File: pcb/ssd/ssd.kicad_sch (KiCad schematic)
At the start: 0 parts

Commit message: 将USB电源升级为5-12V双路DCDC
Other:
- note added: "USB-C 接口与电源 5～12V 输入、5V / 3.3V DCDC"
- note added: "主控：STM32C562CET6，LQFP48，512KB 闪存 / 128KB 运行内存。 VBUS 按外部 5～12V 输入设计；标准 5V USB 连接可用于 ROM DFU。"
- note removed: "USB-C 接口与电源 5V 输入、3.3V 稳压"
- note removed: "主控：STM32C562CET6，LQFP48，512KB 闪存 / 128KB 运行内存。 USB-C 同时用于 5V 供电和出厂引导程序 USB DFU 烧录。"
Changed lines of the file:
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@@
 	(title_block
 		(title "STM32C562 温度与流量显示系统")
-		(date "2026-09-16")
-		(rev "A2")
+		(date "2026-09-18")
+		(rev "A3")
 		(company "温度与流量显示项目")
-		(comment 1 "STM32C562 最小系统与外围电路；全部电阻、电容采用 0603")
+		(comment 1 "常规阻容采用 0603；DCDC 储能电容采用 1206")
 	)
 	(polyline
@@
 		)
 	)
-	(text "主控：STM32C562CET6，LQFP48，512KB 闪存 / 128KB 运行内存。\nUSB-C 同时用于 5V 供电和出厂引导程序 USB DFU 烧录。"
+	(text "主控：STM32C562CET6，LQFP48，512KB 闪存 / 128KB 运行内存。\nVBUS 按外部 5～12V 输入设计；标准 5V USB 连接可用于 ROM DFU。"
 		(exclude_from_sim no)
 		(at 20 33 0)
@@
 		)
 	)
-	(text "USB-C 接口与电源\n5V 输入、3.3V 稳压"
+	(text "USB-C 接口与电源\n5～12V 输入、5V / 3.3V DCDC"
 		(exclude_from_sim no)
 		(at 31.75 78.74 0)

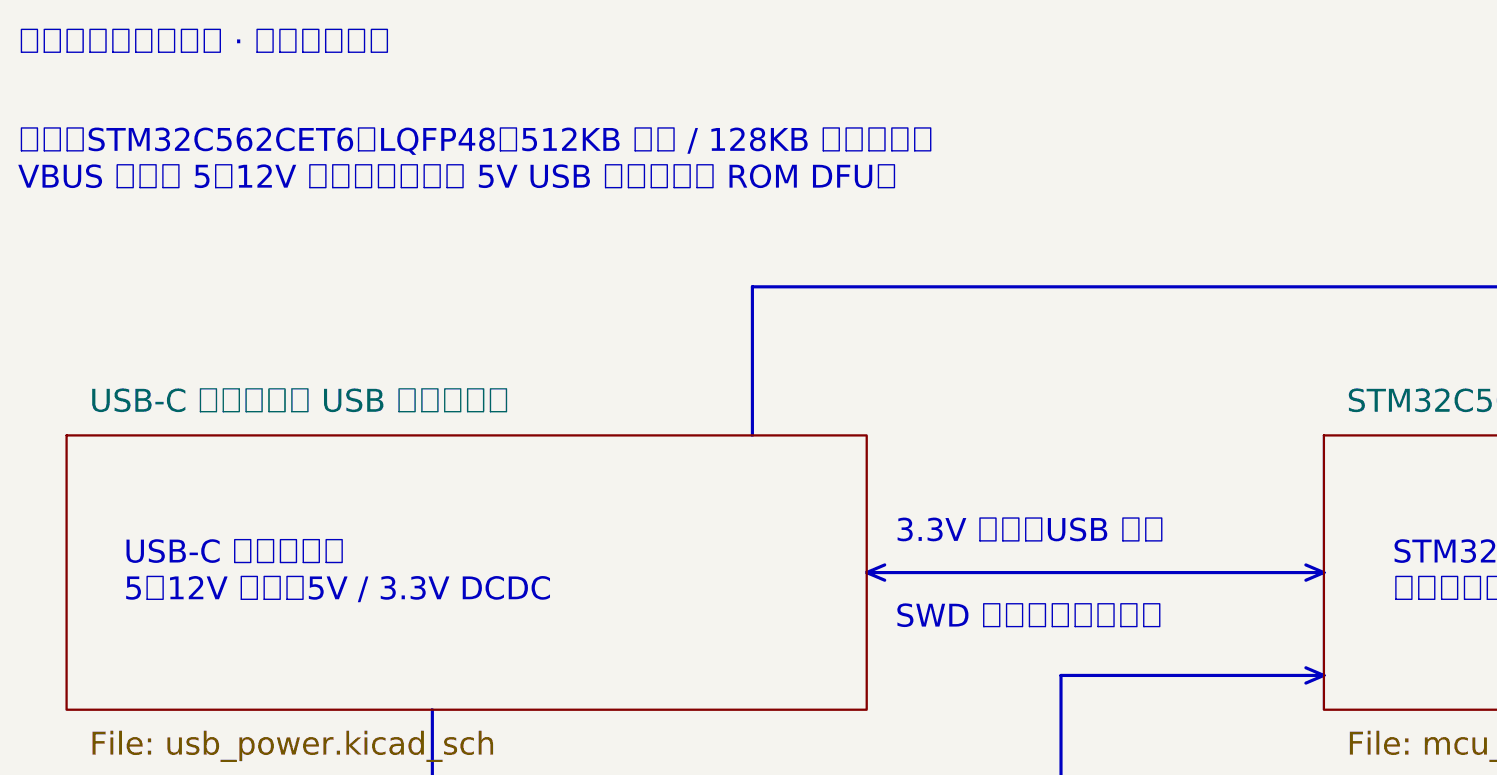
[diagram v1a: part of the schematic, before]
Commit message: 更新 Type-C 供电与 J-Link 调试设计
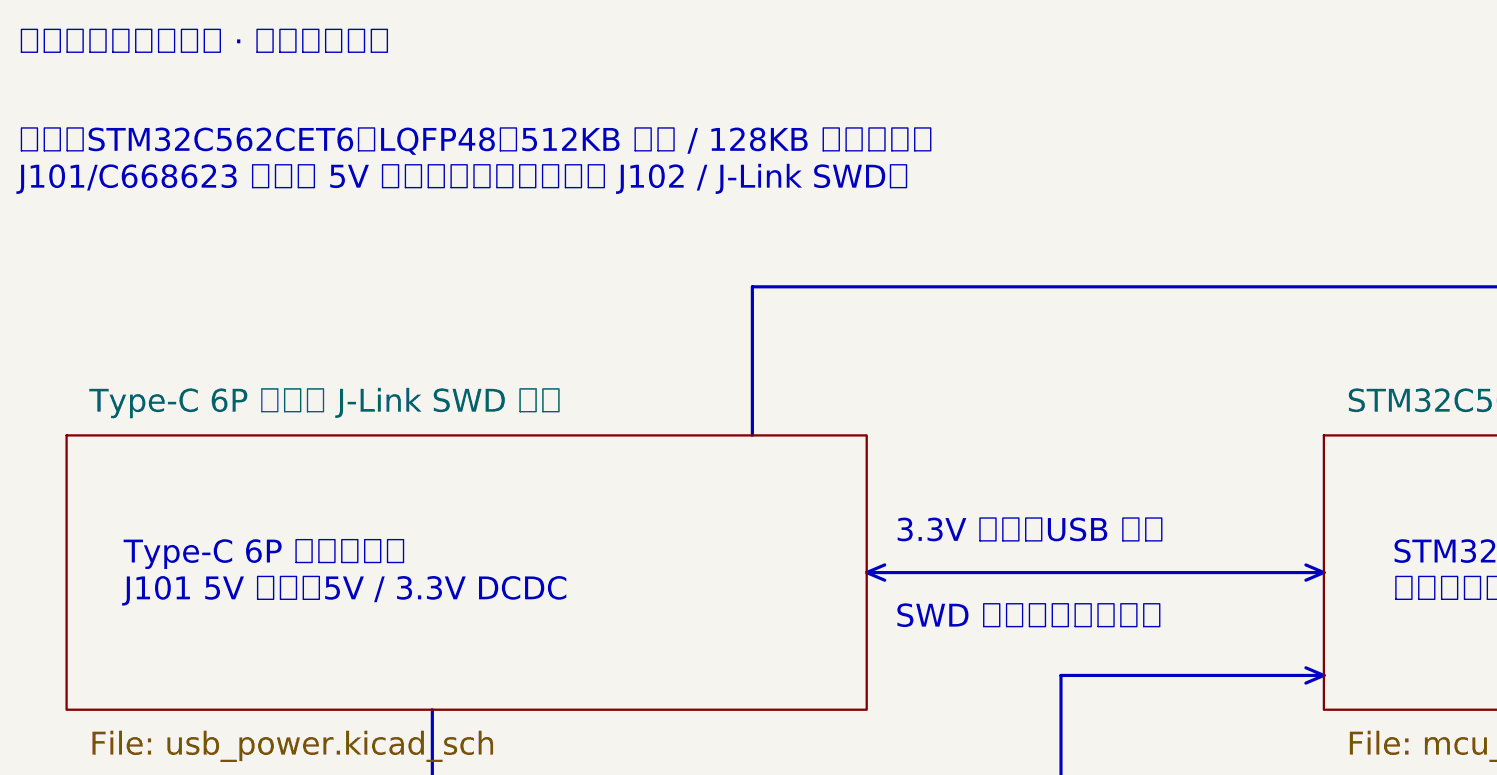
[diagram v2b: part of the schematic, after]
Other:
- sheet USB-C 供电、原生 USB 烧录与调试 renamed Type-C 6P 供电与 J-Link SWD 调试
- note added: "Type-C 6P 仅供电接口 J101 5V 输入、5V / 3.3V DCDC"
- note added: "主控：STM32C562CET6，LQFP48，512KB 闪存 / 128KB 运行内存。 J101/C668623 仅允许 5V 供电；下载与调试使用 J102 / J-Link SWD。"
- note removed: "USB-C 接口与电源 5～12V 输入、5V / 3.3V DCDC"
- note removed: "主控：STM32C562CET6，LQFP48，512KB 闪存 / 128KB 运行内存。 VBUS 按外部 5～12V 输入设计；标准 5V USB 连接可用于 ROM DFU。"
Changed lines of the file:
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@@
 		(effects
 			(font
-				(face "Noto Sans CJK SC")
 				(size 2.54 2.54)
 			)
@@
 		(effects
 			(font
-				(face "Noto Sans CJK SC")
 				(size 2.54 2.54)
 			)
@@
 		(effects
 			(font
-				(face "Noto Sans CJK SC")
 				(size 2.54 2.54)
 			)
@@
 		(effects
 			(font
-				(face "Noto Sans CJK SC")
-				(size 2.54 2.54)
-			)
-			(justify left)
-		)
-	)
-	(text "主控：STM32C562CET6，LQFP48，512KB 闪存 / 128KB 运行内存。\nVBUS 按外部 5～12V 输入设计；标准 5V USB 连接可用于 ROM DFU。"
+				(size 2.54 2.54)
+			)
+			(justify left)
+		)
+	)
+	(text "主控：STM32C562CET6，LQFP48，512KB 闪存 / 128KB 运行内存。\nJ101/C668623 仅允许 5V 供电；下载与调试使用 J102 / J-Link SWD。"
 		(exclude_from_sim no)
 		(at 20 33 0)
 		(effects
 			(font
-				(face "Noto Sans CJK SC")
 				(size 2.54 2.54)
 			)
@@
 		(effects
 			(font
-				(face "Noto Sans CJK SC")
 				(size 2.54 2.54)
 			)
@@
 		(effects
 			(font
-				(face "Noto Sans CJK SC")
 				(size 2.54 2.54)
 			)
@@
 		(effects
 			(font
-				(face "Noto Sans CJK SC")
 				(size 2.54 2.54)
 			)
@@
 		(effects
 			(font
-				(face "Noto Sans CJK SC")
 				(size 2.54 2.54)
 			)
@@
 		(effects
 			(font
-				(face "Noto Sans CJK SC")
-				(size 2.54 2.54)
-			)
-			(justify left)
-		)
-	)
-	(text "USB-C 接口与电源\n5～12V 输入、5V / 3.3V DCDC"
+				(size 2.54 2.54)
+			)
+			(justify left)
+		)
+	)
+	(text "Type-C 6P 仅供电接口\nJ101 5V 输入、5V / 3.3V DCDC"
 		(exclude_from_sim no)
 		(at 31.75 78.74 0)
 		(effects
 			(font
-				(face "Noto Sans CJK SC")
 				(size 2.54 2.54)
 			)
@@
 		(effects
 			(font
-				(face "Noto Sans CJK SC")
 				(size 2.54 2.54)
 			)
@@
 			(effects
 				(font
-					(face "Noto Sans CJK SC")
 					(size 2.54 2.54)
 				)
@@
 			(color 0 0 0 0)
 		)
-		(property "Sheetname" "USB-C 供电、原生 USB 烧录与调试"
+		(property "Sheetname" "Type-C 6P 供电与 J-Link SWD 调试"
 			(at 27.94 59.69 0)
 			(show_name no)
@@
 			(effects
 				(font
-					(face "Noto Sans CJK SC")
 					(size 2.54 2.54)
 				)
@@
 			(effects
 				(font
-					(face "Noto Sans CJK SC")
 					(size 2.54 2.54)
 				)
@@
 			(effects
 				(font
-					(face "Noto Sans CJK SC")
-					(size 2.54 2.54)
-				)
+					(size 2.54 2.54)
+				)
